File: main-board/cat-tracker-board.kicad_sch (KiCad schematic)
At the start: 29 parts, among them J1 Conn_01x10, J3 USB_B_Micro, Q1 SI3443DDV-T1-GE3, SW1 PCM12SMTR, U1 ATSAMD21E18A-M, U3 L80-R, U4 RFM95W-915S2, U5 MCP73831-2ACI/MC, U6 MCP1700T-3602E/TT

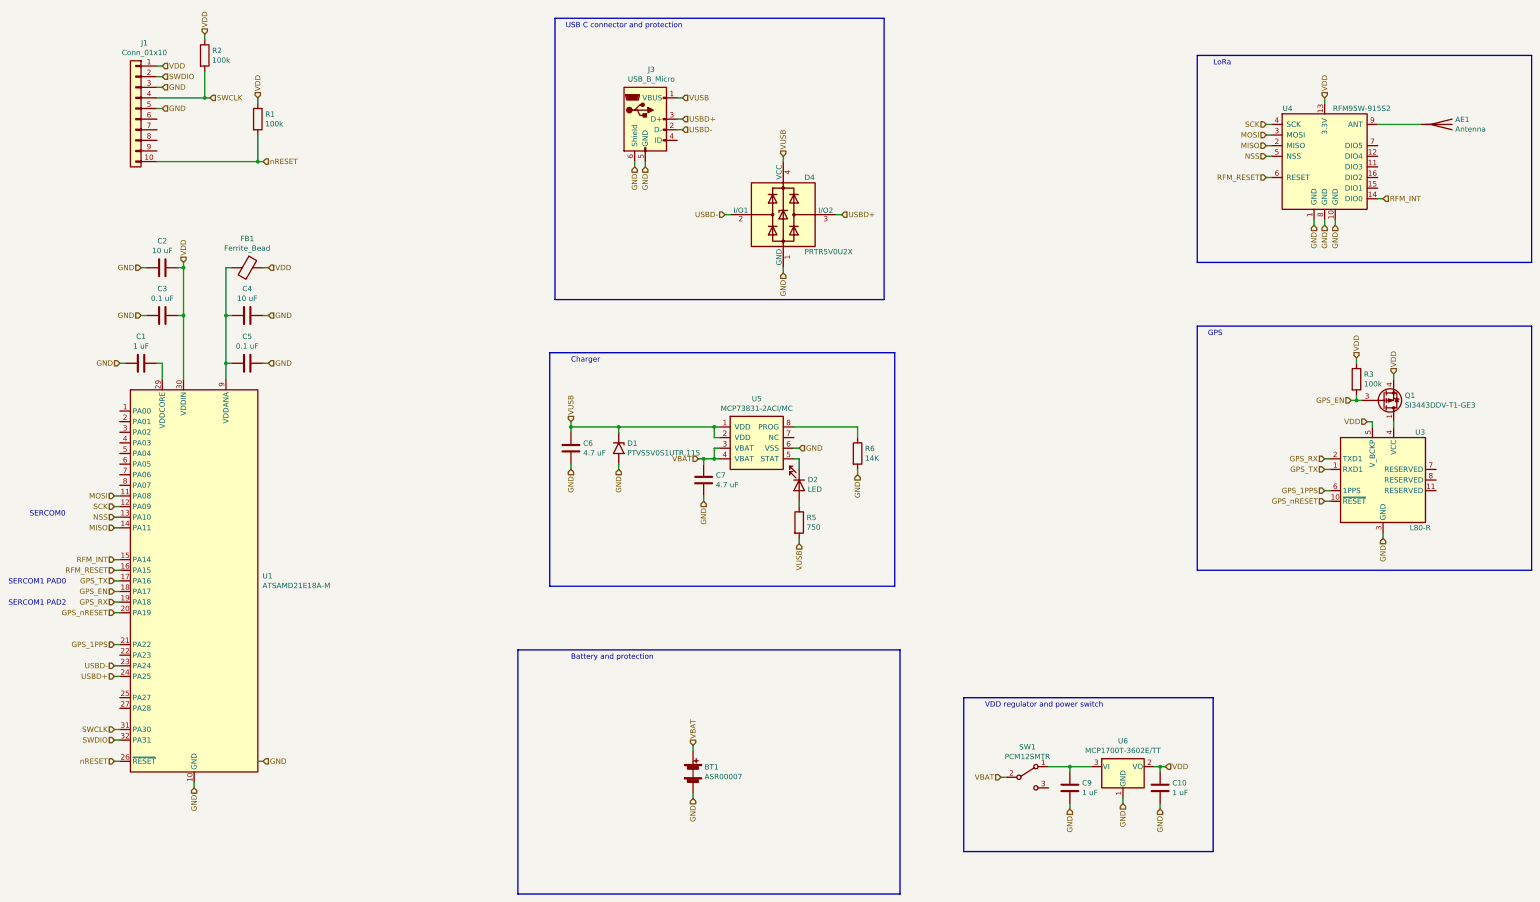
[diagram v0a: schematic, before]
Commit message: Add antenna matching, update some PNs
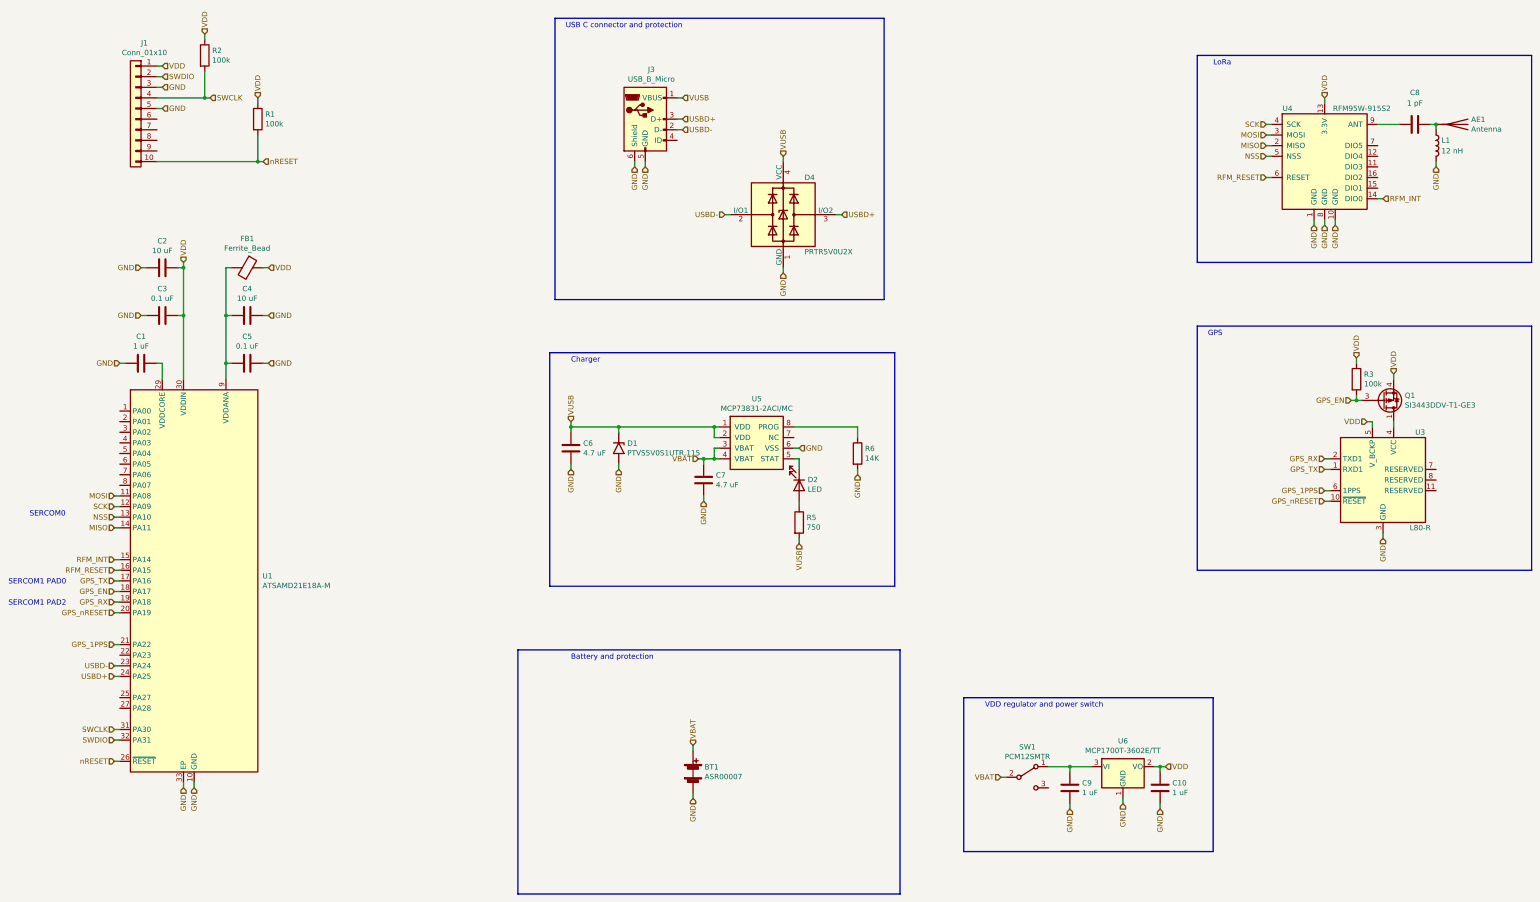
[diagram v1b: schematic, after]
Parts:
- added C8: 1 pF, Capacitor_SMD:C_0603_1608Metric, symbol Device:C
- added L1: 12 nH, Inductor_SMD:L_0603_1608Metric, symbol Device:L
- AE1: exclude (none) -> yes
- C1, C10, C9: description MLCC, 1 uF, 16 V, X7R, 0603 -> MLCC, 1 uF, 25 V, X7R, 0603; mfg1 TDK -> Samsung Electro-Mechanics; mfg1pn CGA3E1X7R1C105K080AC -> CL10B105KA8NNNL
- C3, C5: description MLCC, 0.1 uF, 16 V, X7R, 0603 -> MLCC, 0.1 uF, 50 V, X7R, 0603; mfg1 KEMET -> Samsung Electro-Mechanics; mfg1pn C0603C104M4RAC7411 -> CL10B104KB8NNNL
- C6, C7: description MLCC, 4.7 uF, 16 V, X5R, 0603 -> MLCC, 4.7 uF, 16 V, X7R, 0603; mfg1 TDK -> Murata Electronics; mfg1pn C1608X5R1C475K080AE -> GRM188Z71C475KE21D
- U1: symbol cat-tracker-board-rescue:ATSAMD21E18A-M-MCU_Microchip_SAMD -> MCU_Microchip_SAMD:ATSAMD21E18A-M
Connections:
- net GND: now also L1.2
- net at U4.9 (ANT): now also C8.1; no longer AE1.1 (A)
- new net: AE1.1 (A), C8.2, L1.1
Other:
- moved on the sheet: AE1

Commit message: Add alternate for GPS
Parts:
- U3: mfg2 (none) -> Quectel; mfg2pn (none) -> L80-M39
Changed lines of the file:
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@@
+      (effects (font (size 1.27 1.27)) hide)
+    )
+    (property "mfg2pn" "L80-M39" (id 6) (at 349.25 135.89 0)
+      (effects (font (size 1.27 1.27)) hide)
+    )
+    (property "mfg2" "Quectel" (id 7) (at 349.25 135.89 0)
       (effects (font (size 1.27 1.27)) hide)
     )

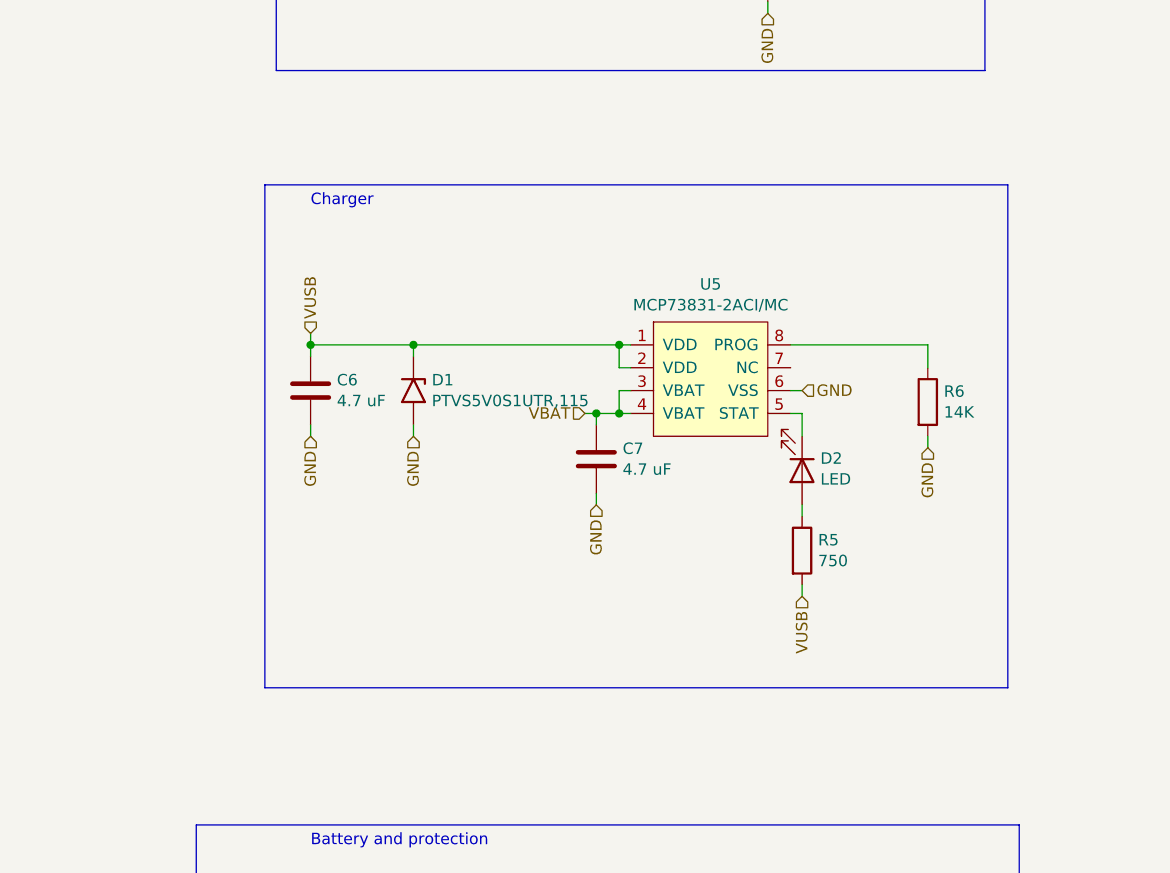
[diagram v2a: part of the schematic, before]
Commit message: Start changing to MCP73838
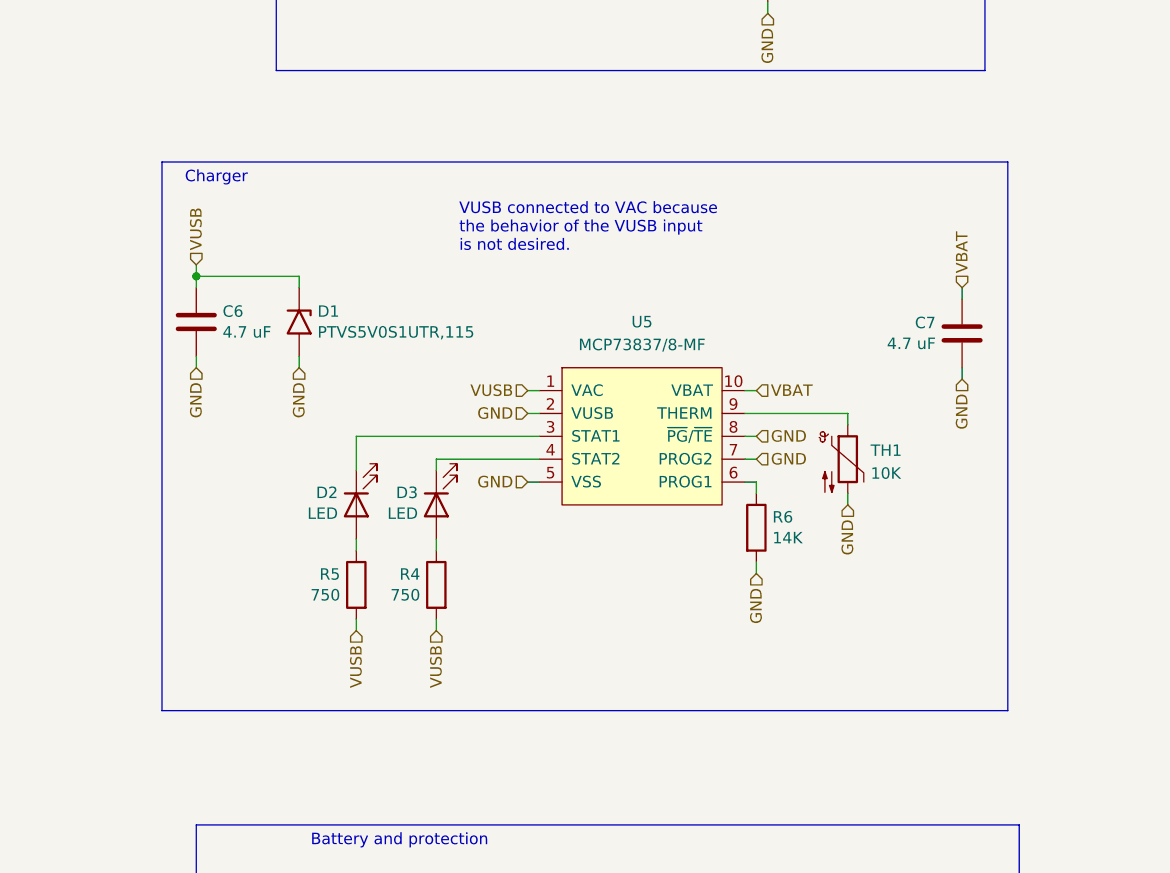
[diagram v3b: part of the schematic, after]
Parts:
- removed U5: MCP73831-2ACI/MC, Package_DFN_QFN:DFN-8-1EP_3x2mm_P0.5mm_EP1.75x1.45mm, symbol colinholzman:MCP7383*-*-MC
- added D3: LED, LED_SMD:LED_0603_1608Metric, symbol Device:LED
- added R4: 750, Resistor_SMD:R_0603_1608Metric, symbol Device:R
- added TH1: 10K, Resistor_SMD:R_0603_1608Metric, symbol Device:Thermistor_NTC
- added U5: MCP73837/8-MF, Package_DFN_QFN:DFN-10-1EP_3x3mm_P0.5mm_EP1.7x2.5mm, symbol colinholzman:MCP73837/8-MF
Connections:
- net GND: now also TH1.2, U5.11 (VSS), U5.2 (VUSB), U5.5 (VSS), U5.7 (PROG2), U5.8 (~{PG}/~{TE})
- net VBAT: now also U5.10 (VBAT)
- net VUSB: now also R4.2, U5.1 (VAC)
- net at D2.1 (K): now also U5.3 (STAT1)
- net at R6.1: now also U5.6 (PROG1)
- new net: TH1.1, U5.9 (THERM)
- new net: D3.2 (A), R4.1
- new net: D3.1 (K), U5.4 (STAT2)
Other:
- note added: "VUSB connected to VAC because the behavior of the VUSB input is not desired."
- moved on the sheet: C6, C7, D1, D2, R5, R6

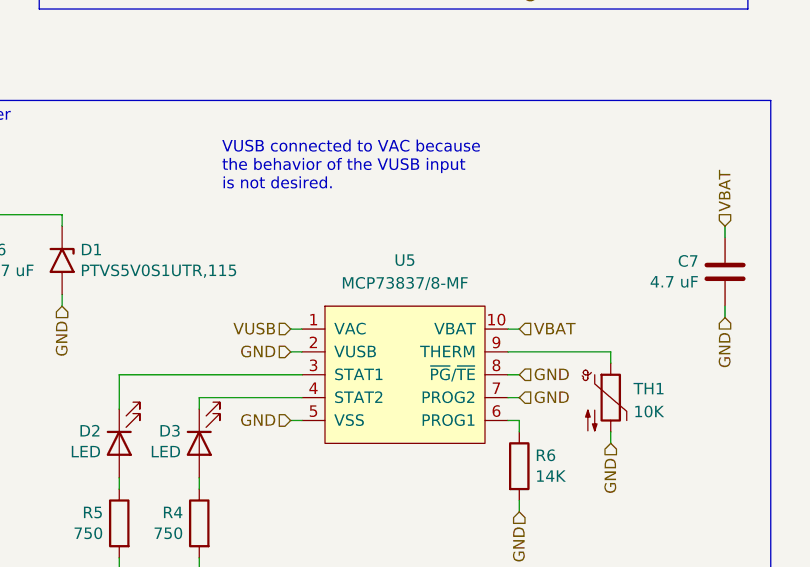
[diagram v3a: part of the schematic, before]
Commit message: Fixed charger symbol
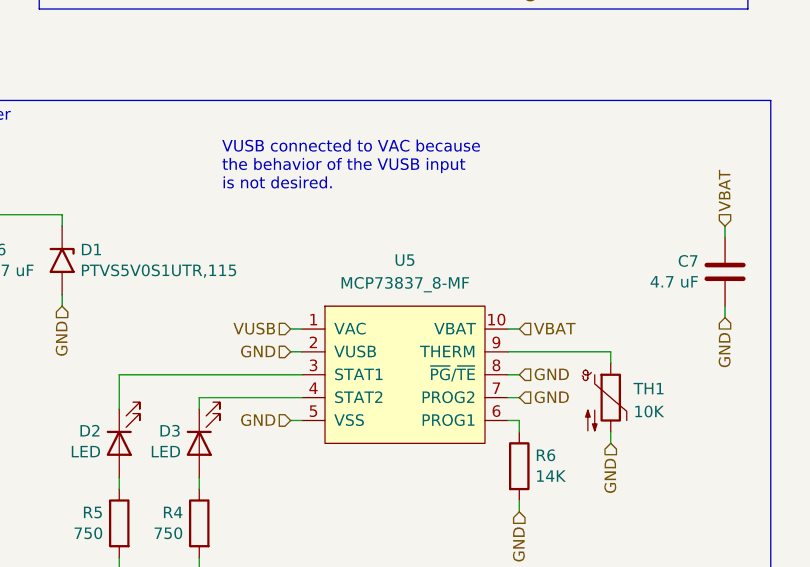
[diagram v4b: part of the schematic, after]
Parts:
- U5: value MCP73837/8-MF -> MCP73837_8-MF; symbol colinholzman:MCP73837/8-MF -> colinholzman:MCP73837_8-MF
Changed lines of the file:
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@@
     (pin "2")
   )
-  (symbol (lib_id "colinholzman:MCP73837/8-MF") (at 191.77 132.08 0) (unit 1)
+  (symbol (lib_id "colinholzman:MCP73837_8-MF") (at 191.77 132.08 0) (unit 1)
     (in_bom yes) (on_board yes) (fields_autoplaced)
     (property "Reference" "U5" (id 0) (at 191.77 120.65 0))
-    (property "Value" "MCP73837/8-MF" (id 1) (at 191.77 123.19 0))
+    (property "Value" "MCP73837_8-MF" (id 1) (at 191.77 123.19 0))
     (property "Footprint" "Package_DFN_QFN:DFN-10-1EP_3x3mm_P0.5mm_EP1.7x2.5mm" (id 2) (at 191.77 143.51 0)
       (effects (font (size 1.27 1.27)) hide)
@@
     )
     (path "/a1fe7c02-942c-4c08-97d9-5ea85d13c90d"
-      (reference "U5") (unit 1) (value "MCP73837/8-MF") (footprint "Package_DFN_QFN:DFN-10-1EP_3x3mm_P0.5mm_EP1.7x2.5mm")
+      (reference "U5") (unit 1) (value "MCP73837_8-MF") (footprint "Package_DFN_QFN:DFN-10-1EP_3x3mm_P0.5mm_EP1.7x2.5mm")
     )
     (path "/00000000-0000-0000-0000-000060e5e54d"

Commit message: Update bom
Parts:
- R1, R2, R3: mfg1 Panasonic -> Bourns; mfg1pn ERJ-3EKF1003V -> CR0603-FX-1003ELF
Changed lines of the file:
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@@
       (effects (font (size 1.27 1.27)) hide)
     )
-    (property "mfg1" "Panasonic" (id 4) (at 67.31 34.29 0)
-      (effects (font (size 1.27 1.27)) hide)
-    )
-    (property "mfg1pn" "ERJ-3EKF1003V" (id 5) (at 67.31 34.29 0)
+    (property "mfg1" "Bourns" (id 4) (at 67.31 34.29 0)
+      (effects (font (size 1.27 1.27)) hide)
+    )
+    (property "mfg1pn" "CR0603-FX-1003ELF" (id 5) (at 67.31 34.29 0)
       (effects (font (size 1.27 1.27)) hide)
     )
@@
       (effects (font (size 1.27 1.27)) hide)
     )
-    (property "mfg1" "Panasonic" (id 4) (at 80.01 49.53 0)
-      (effects (font (size 1.27 1.27)) hide)
-    )
-    (property "mfg1pn" "ERJ-3EKF1003V" (id 5) (at 80.01 49.53 0)
+    (property "mfg1" "Bourns" (id 4) (at 80.01 49.53 0)
+      (effects (font (size 1.27 1.27)) hide)
+    )
+    (property "mfg1pn" "CR0603-FX-1003ELF" (id 5) (at 80.01 49.53 0)
       (effects (font (size 1.27 1.27)) hide)
     )
@@
       (effects (font (size 1.27 1.27)) hide)
     )
-    (property "mfg1" "Panasonic" (id 4) (at 342.9 111.76 0)
-      (effects (font (size 1.27 1.27)) hide)
-    )
-    (property "mfg1pn" "ERJ-3EKF1003V" (id 5) (at 342.9 111.76 0)
-      (effects (font (size 1.27 1.27)) hide)
-    )
+    (property "mfg1" "Bourns" (id 4) (at 342.9 111.76 0)
+      (effects (font (size 1.27 1.27)) hide)
+    )
+    (property "mfg1pn" "CR0603-FX-1003ELF" (id 5) (at 342.9 111.76 0)
+      (effects (font (size 1.27 1.27)) hide)
+    )
